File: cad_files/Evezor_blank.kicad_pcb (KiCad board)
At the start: 2 copper layers, 49 x 65 mm, 36 parts, among them J1 USB_C_Receptacle_USB2.0, J2 RJ11, J3 RJ11, J4 PH, J5 PH, J6 Conn_02x03_Odd_Even, SW1 SW_Push, U1 SY8401ABC, U2 AMS1117-3.3, U3 EDGE_STM32F405_CPU_V1

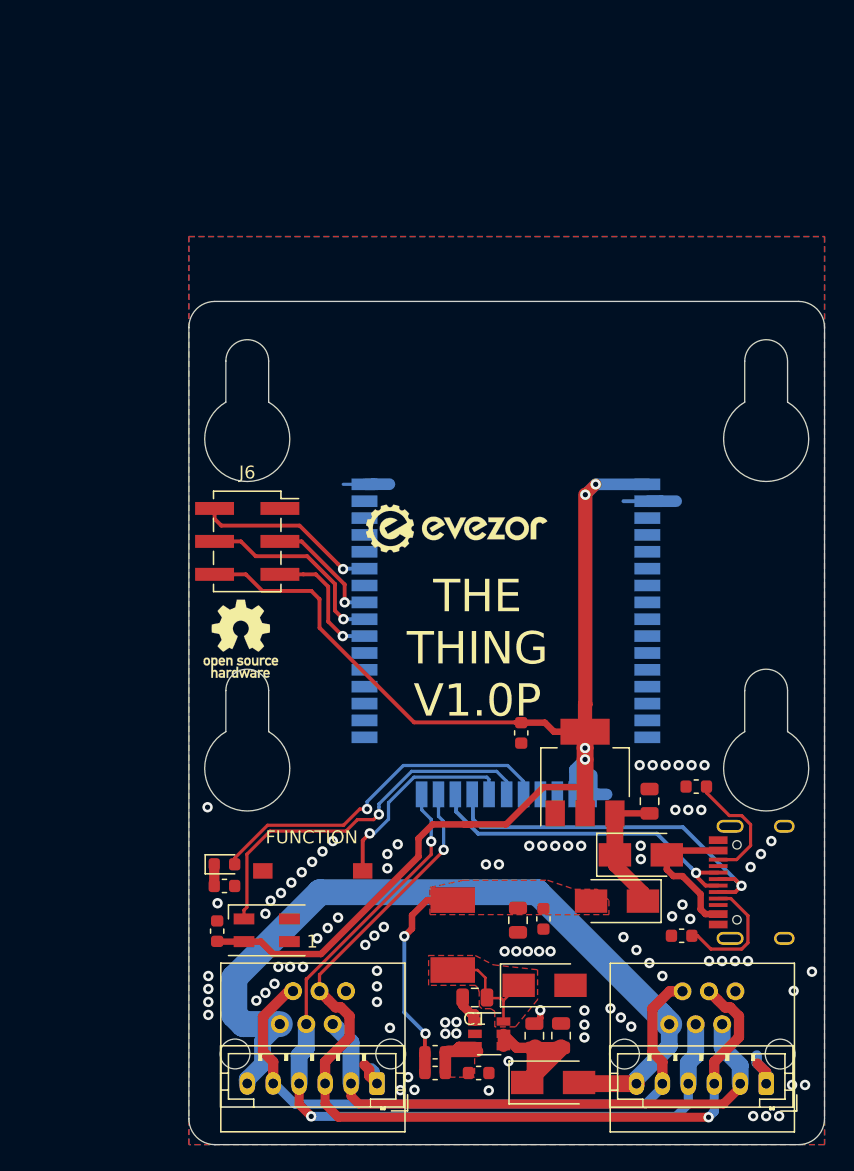
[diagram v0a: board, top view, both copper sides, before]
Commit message: add esp/ usb/ status lights and buttons
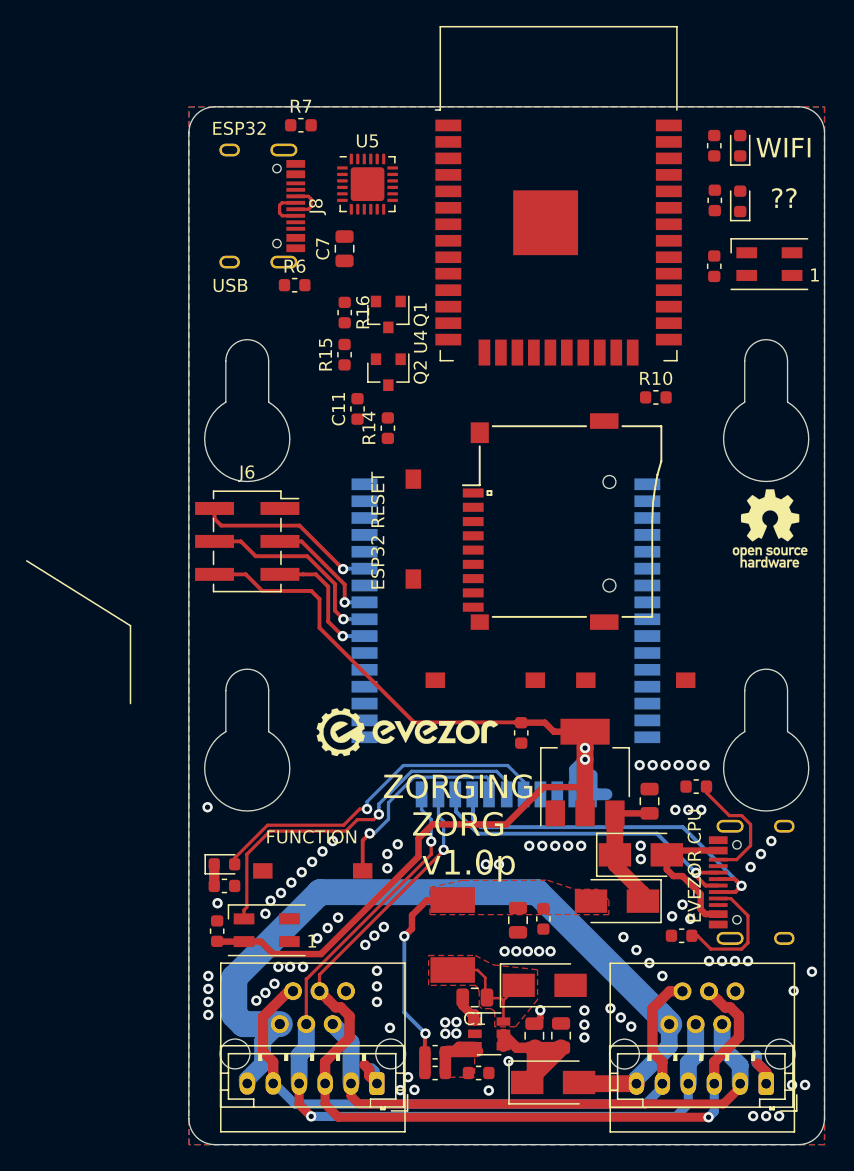
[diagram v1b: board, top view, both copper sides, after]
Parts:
- added C11: 1uF, Capacitor_SMD:C_0603_1608Metric, F.Cu at (113.5, 94.3)
- added C12: .1uF, Capacitor_SMD:C_0603_1608Metric, F.Cu at (141.0, 83.3)
- added C7: 10uF, Capacitor_SMD:C_0805_2012Metric, F.Cu at (112.5, 81.9)
- added D7: LED, LED_SMD:LED_0603_1608Metric, F.Cu at (143.0, 78.3)
- added D8: LED, LED_SMD:LED_0603_1608Metric, F.Cu at (143.0, 74.0)
- added D9: SK6812MINI, LED_SMD:LED_SK6812MINI_PLCC4_3.5x3.5mm_P1.75mm, F.Cu at (145.2, 83.1)
- added J8: USB_C_Receptacle_USB2.0, EvezorLIB:USB_C_Receptacle_HRO_TYPE-C-31-M-12, F.Cu at (104.7, 78.7)
- added Q1: MMBT2222, Package_TO_SOT_SMD:SOT-23, F.Cu at (115.9, 87.0)
- added Q2: MMBT2222, Package_TO_SOT_SMD:SOT-23, F.Cu at (115.9, 91.5)
- added R10: 10k, Resistor_SMD:R_0603_1608Metric, F.Cu at (136.5, 93.4)
- added R14: 10k, Resistor_SMD:R_0603_1608Metric, F.Cu at (115.8, 95.8)
- added R15: 10k, Resistor_SMD:R_0603_1608Metric, F.Cu at (112.5, 90.1)
- added R16: 10k, Resistor_SMD:R_0603_1608Metric, F.Cu at (112.5, 86.9)
- added R17: 15k, Resistor_SMD:R_0603_1608Metric, F.Cu at (141.0, 78.2)
- added R18: 15k, Resistor_SMD:R_0603_1608Metric, F.Cu at (141.0, 74.0)
- added R6: 5.1k, Resistor_SMD:R_0603_1608Metric, F.Cu at (108.7, 84.8)
- added R7: 5.1k, Resistor_SMD:R_0603_1608Metric, F.Cu at (109.1, 72.4)
- added SW2: SW_Push, EvezorLIB:SWITCH_2x3_SMD_TACTILE_GREEN, F.Cu at (117.8, 103.5)
- added SW3: SW_Push, EvezorLIB:SWITCH_2x3_SMD_TACTILE_GREEN, F.Cu at (123.3, 115.2)
- added SW4: SW_Push, EvezorLIB:SWITCH_2x3_SMD_TACTILE_GREEN, F.Cu at (134.9, 115.2)
- added U4: ESP32-WROOM-32D, RF_Module:ESP32-WROOM-32, F.Cu at (129.0, 80.7)
- added U5: CP2104, Package_DFN_QFN:QFN-24-1EP_4x4mm_P0.5mm_EP2.6x2.6mm, F.Cu at (114.3, 77.0)
- added XS1: uSD-push_push_SMD, Evezor_extras:Conn_uSDcard, F.Cu at (132.9, 103.0)
- moved REF** 41.7 mm to (145.3, 103.5)
- moved G*** 16.2 mm to (112.2, 119.2)
- moved G*** 16.2 mm to (119.5, 119.2)
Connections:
- U3 pad 4: Net-(U3-Pad4) -> /VSPI_CS
- U3 pad 5: Net-(U3-Pad5) -> /VPSI_CLK
- U3 pad 6: Net-(U3-Pad6) -> /VSPI_MISO
- U3 pad 7: Net-(U3-Pad7) -> /VSPI_MOSI
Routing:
- net +3V3: track 107.4 -> 82.8 mm, vias 4 -> 2
- net GND: track 18.9 -> 12.1 mm
- net /ESP_D+: track 0.00 -> 3.26 mm
- net /ESP_D-: track 0.00 -> 3.12 mm
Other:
- board size 49 x 65 mm -> 49 x 80 mm
- board text added: "??"
- board text added: "ESP32"
- board text added: "ESP32 RESET"
- board text added: "EVEZOR CPU"
- board text added: "USB"
- board text added: "WIFI"
- board text added: "ZORGING ZORG"
- board text added: "v1.0p"
- board text removed: "THE THING V1.0P"
